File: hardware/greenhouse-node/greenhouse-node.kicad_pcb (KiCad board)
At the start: 2 copper layers, 90.2 x 69.8 mm, 49 parts, among them J1 Conn_01x12_Male, J2 Conn_01x02_Male, J3 Conn_01x02_Male, J4 Conn_01x02_Male, J5 Conn_01x04_Male, J6 RX_PinHeader_1x04_P2.54mm, J7 TX_PinHeader_1x04_P2.54mm, J8 Conn_01x02_Male, Q1 BC549C, Q2 BC549C, Q3 BC549C, Q4 IRF9530N, Q5 IRF530N, Q6 IRF9530N, Q7 IRF530N, Q8 BC549C, Q9 BC549C, U1 ATtiny84A-P, U2 L7805, U3 74HC595

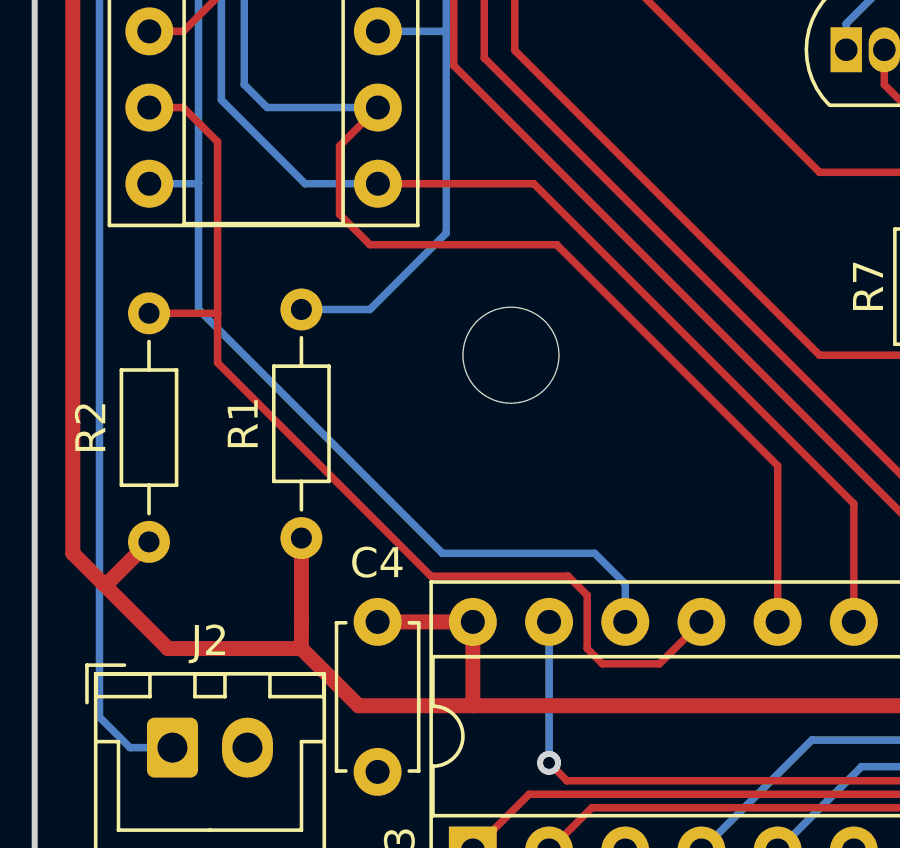
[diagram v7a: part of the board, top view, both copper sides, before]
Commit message: Shorten trace
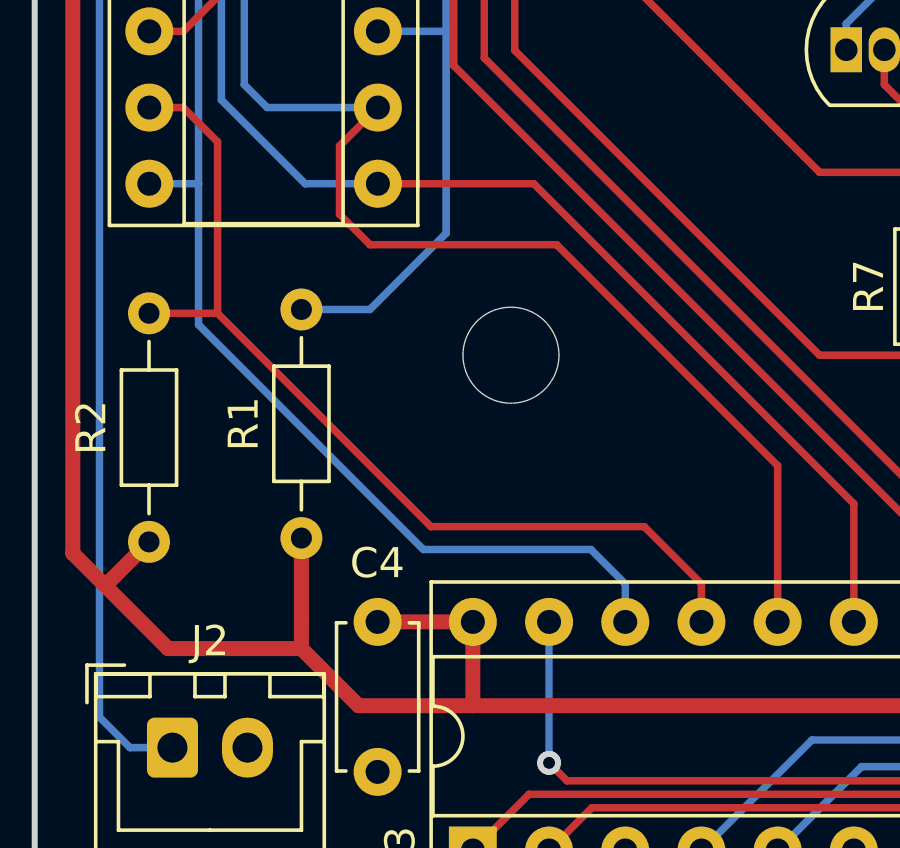
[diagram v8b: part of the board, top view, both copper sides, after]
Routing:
- net /SR_OE: track 34.3 -> 31.9 mm
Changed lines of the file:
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@@
   (segment (start 140.723 59.556) (end 140.723 58.022) (width 0.25) (layer "B.Cu") (net 13))
   (segment (start 135.255 72.0725) (end 131.953 68.7705) (width 0.25) (layer "B.Cu") (net 13))
+  (segment (start 133.731 90.805) (end 133.731 95.504) (width 0.25) (layer "B.Cu") (net 14))
   (segment (start 132.09 90.805) (end 133.731 90.805) (width 0.25) (layer "B.Cu") (net 14))
-  (segment (start 141.859 103.124) (end 146.939 103.124) (width 0.25) (layer "B.Cu") (net 14))
-  (segment (start 133.731 94.996) (end 141.859 103.124) (width 0.25) (layer "B.Cu") (net 14))
+  (segment (start 133.731 95.504) (end 141.224 102.997) (width 0.25) (layer "B.Cu") (net 14))
   (segment (start 135.723 59.476) (end 135.723 58.022) (width 0.25) (layer "B.Cu") (net 14))
-  (segment (start 133.731 90.805) (end 133.731 94.996) (width 0.25) (layer "B.Cu") (net 14))
-  (segment (start 146.939 103.124) (end 147.955 104.14) (width 0.25) (layer "B.Cu") (net 14))
+  (segment (start 141.224 102.997) (end 146.812 102.997) (width 0.25) (layer "B.Cu") (net 14))
   (segment (start 130.683 64.516) (end 135.723 59.476) (width 0.25) (layer "B.Cu") (net 14))
   (segment (start 133.731 90.805) (end 133.731 72.415701) (width 0.25) (layer "B.Cu") (net 14))
   (segment (start 133.731 72.415701) (end 130.683 69.367701) (width 0.25) (layer "B.Cu") (net 14))
   (segment (start 130.683 69.367701) (end 130.683 64.516) (width 0.25) (layer "B.Cu") (net 14))
+  (segment (start 146.812 102.997) (end 147.955 104.14) (width 0.25) (layer "B.Cu") (net 14))
   (segment (start 147.955 104.14) (end 147.955 105.41) (width 0.25) (layer "B.Cu") (net 14))
   (segment (start 144.907 90.805) (end 155.575 101.473) (width 0.25) (layer "F.Cu") (net 15))
@@
   (segment (start 134.493 88.011) (end 134.493 72.263) (width 0.25) (layer "B.Cu") (net 15))
   (segment (start 132.09 88.265) (end 133.223 88.265) (width 0.25) (layer "F.Cu") (net 16))
-  (segment (start 134.366 96.774) (end 141.478 103.886) (width 0.25) (layer "F.Cu") (net 16))
-  (segment (start 134.366 95.123) (end 134.366 96.774) (width 0.25) (layer "F.Cu") (net 16))
-  (segment (start 146.685 104.521) (end 146.685 106.299) (width 0.25) (layer "F.Cu") (net 16))
-  (segment (start 146.05 103.886) (end 146.685 104.521) (width 0.25) (layer "F.Cu") (net 16))
+  (segment (start 134.366 95.123) (end 141.478 102.235) (width 0.25) (layer "F.Cu") (net 16))
+  (segment (start 141.478 102.235) (end 148.59 102.235) (width 0.25) (layer "F.Cu") (net 16))
+  (segment (start 150.495 104.14) (end 150.495 105.41) (width 0.25) (layer "F.Cu") (net 16))
+  (segment (start 148.59 102.235) (end 150.495 104.14) (width 0.25) (layer "F.Cu") (net 16))
   (segment (start 133.223 88.265) (end 134.366 89.408) (width 0.25) (layer "F.Cu") (net 16))
-  (segment (start 146.685 106.299) (end 147.193 106.807) (width 0.25) (layer "F.Cu") (net 16))
-  (segment (start 141.478 103.886) (end 146.05 103.886) (width 0.25) (layer "F.Cu") (net 16))
-  (segment (start 149.098 106.807) (end 150.495 105.41) (width 0.25) (layer "F.Cu") (net 16))
   (segment (start 134.366 95.123) (end 132.08 95.123) (width 0.25) (layer "F.Cu") (net 16))
   (segment (start 134.366 89.408) (end 134.366 95.123) (width 0.25) (layer "F.Cu") (net 16))
-  (segment (start 147.193 106.807) (end 149.098 106.807) (width 0.25) (layer "F.Cu") (net 16))
   (segment (start 139.7 50.78) (end 139.7 54.102) (width 0.25) (layer "B.Cu") (net 17))
   (segment (start 147.32 54.102) (end 139.7 54.102) (width 0.25) (layer "B.Cu") (net 17))
